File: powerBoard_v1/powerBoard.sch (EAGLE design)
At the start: 43 parts, among them IC1 7805T, IC2 317T, IC3 317T, IC4 317T, IC5 7808T, J1 DCJ0202

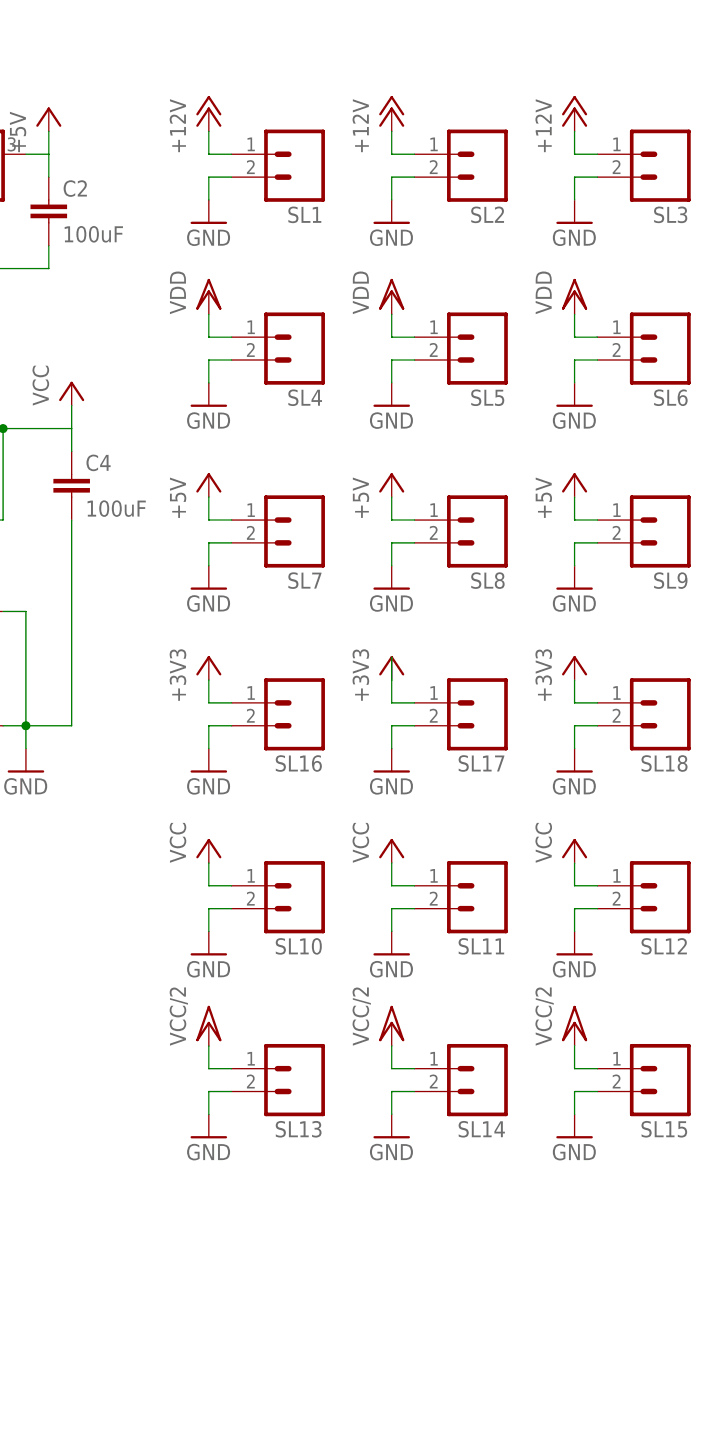
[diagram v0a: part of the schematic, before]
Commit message: powerBoard schematic corrected
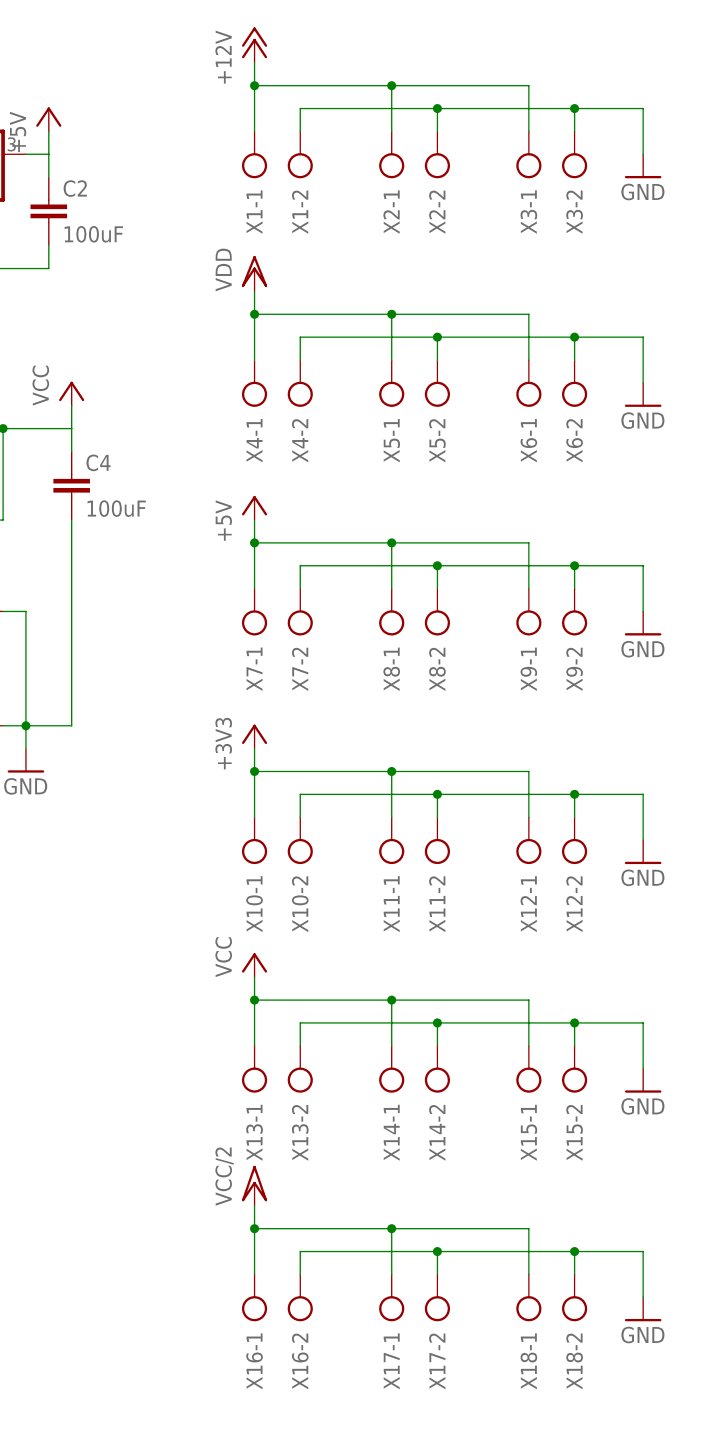
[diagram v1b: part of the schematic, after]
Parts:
- removed SL1, SL10, SL11, SL12, SL13, SL14, SL15, SL16, SL17, SL18, SL2, SL3, SL4, SL5, SL6, SL7, SL8, SL9: (no value), con-amp-quick:M02
- added X1, X10, X11, X12, X13, X14, X15, X16, X17, X18, X2, X3, X4, X5, X6, X7, X8, X9: (no value), con-ptr500:AK300/2
- R12: device pot:TRIM_US-CA6V -> pot:TRIM_US-RJ9W
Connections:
- net +12V: now also X1-1.KL, X2-1.KL, X3-1.KL; no longer SL1.1, SL2.1, SL3.1
- net +3V3: now also X10-1.KL, X11-1.KL, X12-1.KL; no longer SL16.1, SL17.1, SL18.1
- net +5V: now also X7-1.KL, X8-1.KL, X9-1.KL; no longer SL7.1, SL8.1, SL9.1
- net GND: now also X1-2.KL, X10-2.KL, X11-2.KL, X12-2.KL, X13-2.KL, X14-2.KL, X15-2.KL, X16-2.KL, X17-2.KL, X18-2.KL, X2-2.KL, X3-2.KL, X4-2.KL, X5-2.KL, X6-2.KL, X7-2.KL, X8-2.KL, X9-2.KL; no longer SL1.2, SL10.2, SL11.2, SL12.2, SL13.2, SL14.2, SL15.2, SL16.2, SL17.2, SL18.2, SL2.2, SL3.2, SL4.2, SL5.2, SL6.2, SL7.2, SL8.2, SL9.2
- net VCC: now also X13-1.KL, X14-1.KL, X15-1.KL; no longer SL10.1, SL11.1, SL12.1
- net VCC/2: now also X16-1.KL, X17-1.KL, X18-1.KL; no longer SL13.1, SL14.1, SL15.1
- net VDD: now also X4-1.KL, X5-1.KL, X6-1.KL; no longer SL4.1, SL5.1, SL6.1
